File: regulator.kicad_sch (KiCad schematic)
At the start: 20 parts, among them U3 AP62200TWU-7, U4 AP62200TWU-7

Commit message: Ready to restart work!
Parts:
- removed R16: 10k, symbol Device:R
- removed R2: 100k, symbol Device:R
- removed R3: 18k, symbol Device:R
- removed R4: 33k, symbol Device:R
- added R13: 15kΩ, Resistor_SMD:R_0603_1608Metric, symbol !Resistor-0603:15kΩ
- added R2: 20kΩ, Resistor_SMD:R_0603_1608Metric, symbol !Resistor-0603:20kΩ
- added R3: 3.6kΩ, Resistor_SMD:R_0603_1608Metric, symbol !Resistor-0603:3.6kΩ
- added R4: 49.9kΩ, Resistor_SMD:R_0603_1608Metric, symbol !Resistor-0603:49.9kΩ
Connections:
- net +3.3V: now also R4.1
- net +5V: now also R2.1
- net GND: now also R13.2, R3.2
- net at U3.4 (FB): now also R2.2, R3.1
- net at U4.4 (FB): now also R13.1, R4.2

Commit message: Schematic complete (I think)
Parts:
- removed C11, C13, C14, C2, C4, C5: 0.1u, Capacitor_SMD:C_0805_2012Metric, symbol Device:C
- removed C12, C17: 47u, Capacitor_SMD:C_0805_2012Metric, symbol Device:C
- removed C15, C6: 10u, Capacitor_SMD:C_0805_2012Metric, symbol Device:C
- removed C16, C3: 47u, Capacitor_SMD:C_1206_3216Metric, symbol Device:C
- added C10, C6: 10uF, Capacitor_SMD:C_0805_2012Metric, symbol !Capacitor-0805:10uF_X5R_50V
- added C11, C13, C2, C3, C4, C5: 100nF, Capacitor_SMD:C_0603_1608Metric, symbol !Capacitor-0603:100nF_X7R_50V
- added C12, C15, C17, C18: 47uF, Capacitor_SMD:C_0805_2012Metric, symbol !Capacitor-1206:47uF_X5R_10V
- L1, L2: value 6.8uH -> FXL0630-6R8-M; symbol Device:L -> !Inductor-Power:FXL0630-6R8-M; PN FXL0630-6R8-M -> (none)
- U3, U4: symbol motion-sensor-syms:ADP6220x -> !Power Management:AP62200TWU-7
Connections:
- net +3.3V: now also C12.1, C15.1
- net +5V: now also C17.1, C18.1
- net GND: now also C10.2, C11.2, C12.2, C13.2, C15.2, C17.2, C18.2, C2.2, C4.2, C6.2
- net V_{IN}: now also C10.1, C2.1, C4.1, C6.1
- net at L2.1, U4.2 (SW): now also C5.2
- net at U4.6 (BST): now also C5.1
- net at L1.1, U3.2 (SW): now also C3.2
- net at U3.5 (EN): now also C11.1
- net at U3.6 (BST): now also C3.1
- net at U4.5 (EN): now also C13.1

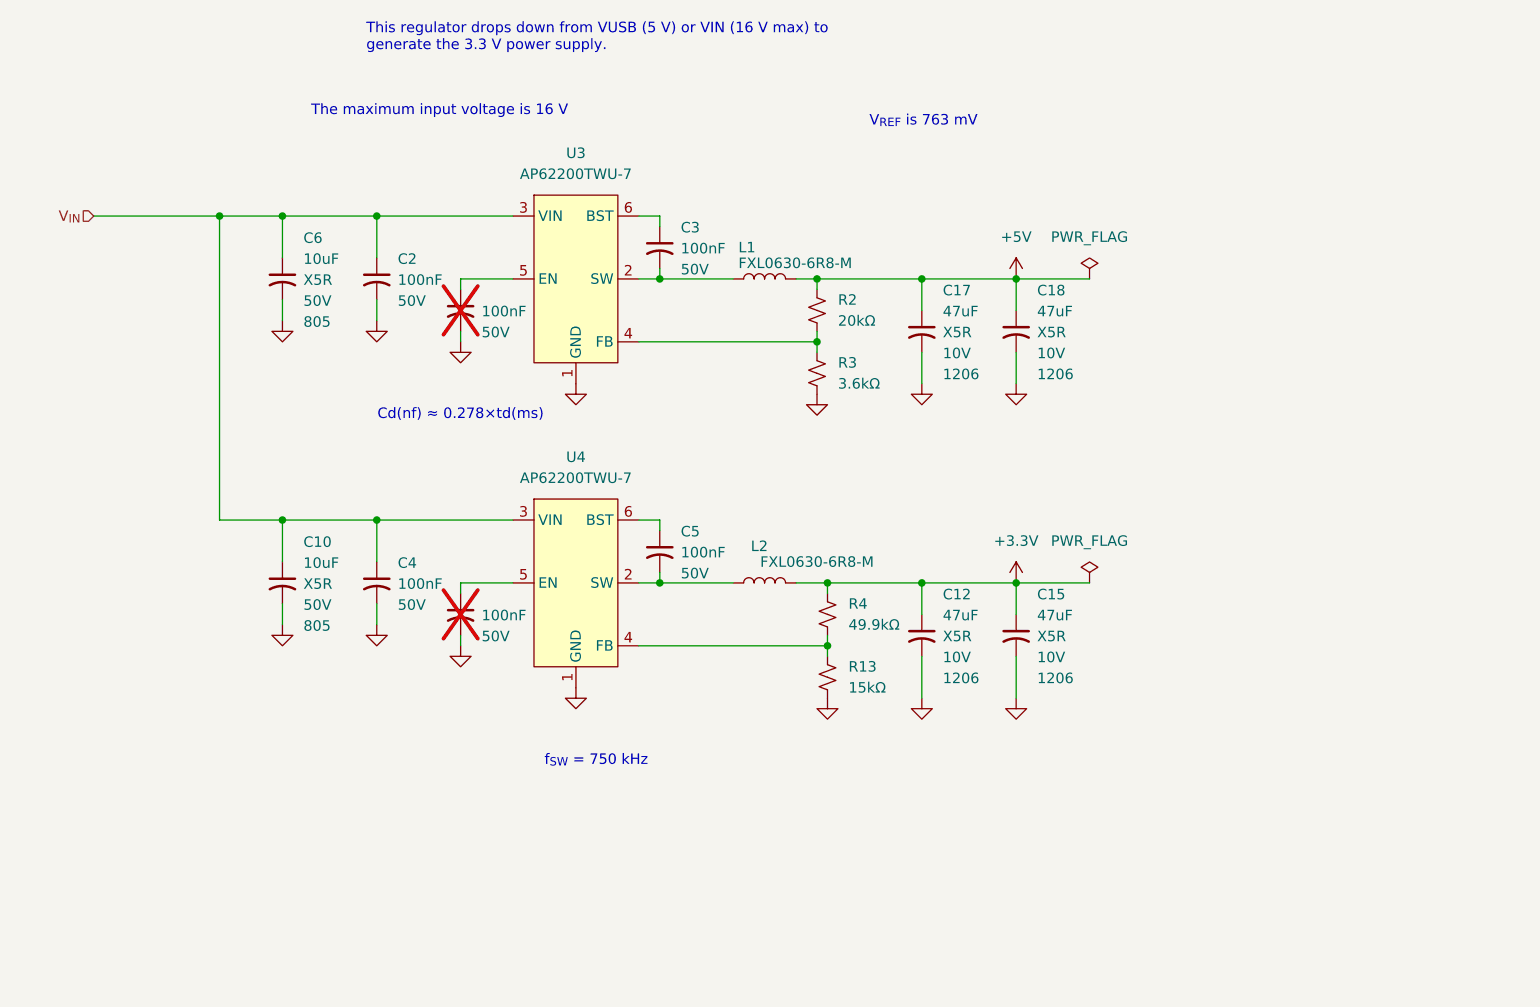
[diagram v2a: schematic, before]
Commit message: Split the two ground planes
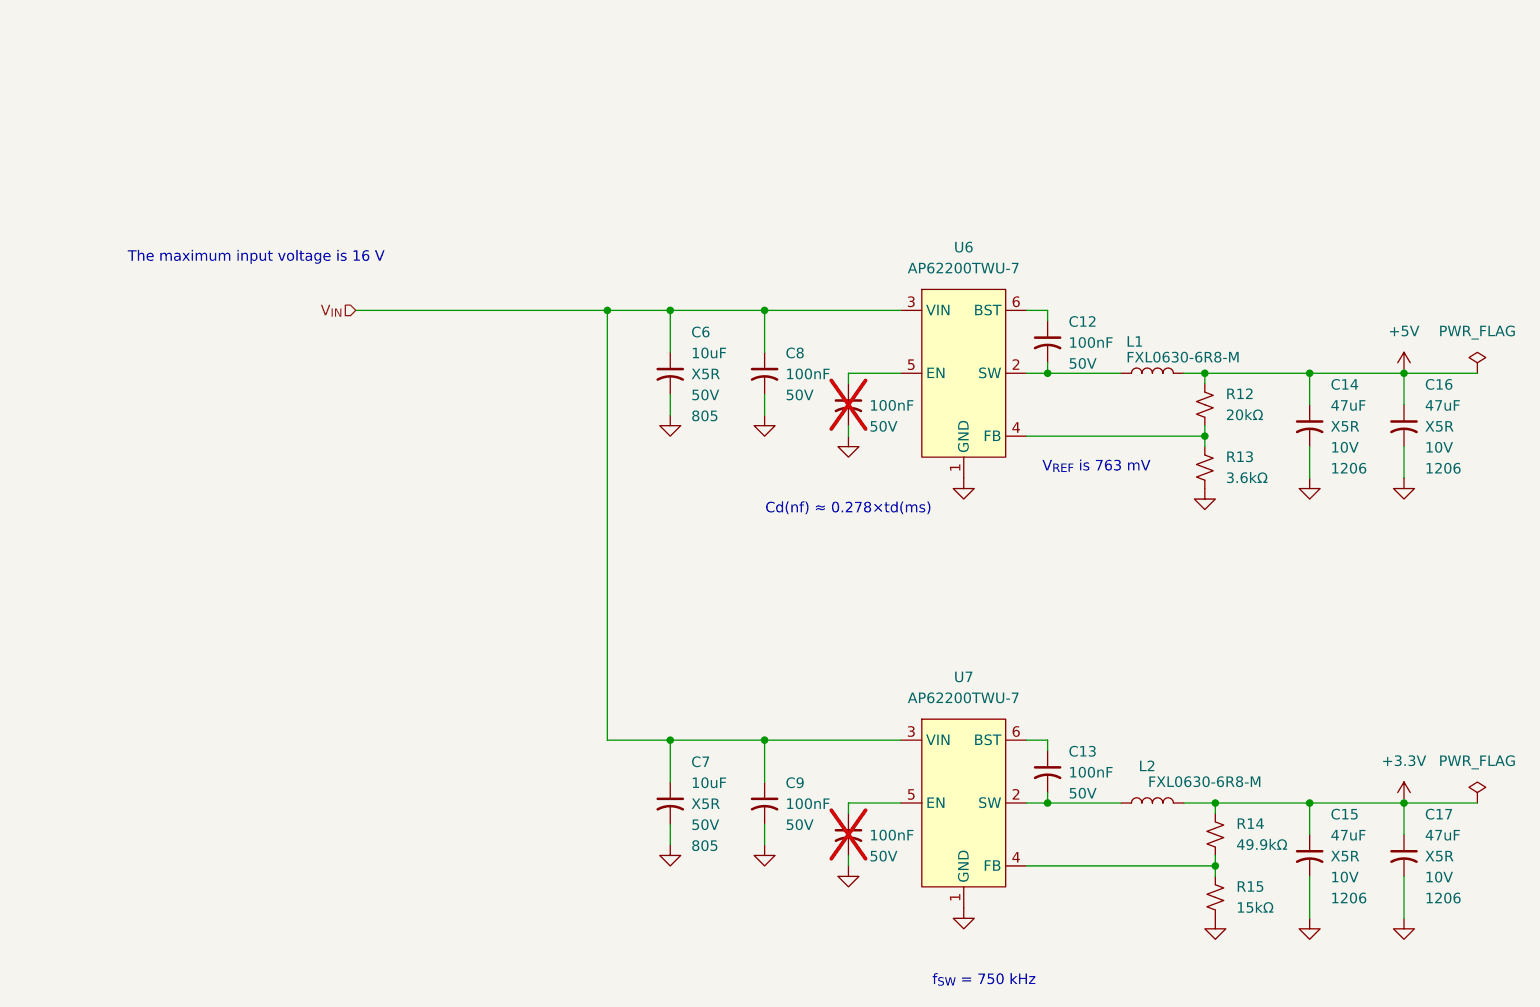
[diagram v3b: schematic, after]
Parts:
- C14: renamed from C17; footprint Capacitor_SMD:C_0805_2012Metric -> Capacitor_SMD:C_1206_3216Metric
- C15: renamed from C12; footprint Capacitor_SMD:C_0805_2012Metric -> Capacitor_SMD:C_1206_3216Metric
- C16: renamed from C18; footprint Capacitor_SMD:C_0805_2012Metric -> Capacitor_SMD:C_1206_3216Metric
- C17: renamed from C15; footprint Capacitor_SMD:C_0805_2012Metric -> Capacitor_SMD:C_1206_3216Metric
- renumbered C11 to C10, C13 to C11, C3 to C12, C5 to C13, C10 to C7, C2 to C8, C4 to C9, R2 to R12, R3 to R13, R4 to R14, R13 to R15, U3 to U6, U4 to U7
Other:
- note removed: "This regulator drops down from VUSB (5 V) or VIN (16 V max) to generate the 3.3 V power supply."
- moved on the sheet: C12, C13, C14, C15, C16, C17, C6, C7, C8, C9, L1, L2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

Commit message: Rev B Submitted
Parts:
- C10, C11, C12, C13, C8, C9: JLCPCB C14663 -> (none); JLCPCB PN (none) -> C14663
- C14, C15, C16, C17: JLCPCB C96123 -> (none); JLCPCB PN (none) -> C96123
- C6, C7: JLCPCB C440198 -> (none); JLCPCB PN (none) -> C440198; Unnamed: 4 (none) -> nan
- L1, L2: JLCPCB C167221 -> (none); JLCPCB PN (none) -> C167221
- R12: JLCPCB C4184 -> (none); JLCPCB PN (none) -> C4184
- R13: JLCPCB C22980 -> (none); JLCPCB PN (none) -> C22980
- R14: JLCPCB C23184 -> (none); JLCPCB PN (none) -> C23184
- R15: JLCPCB C22809 -> (none); JLCPCB PN (none) -> C22809
- U6, U7: FT Rotation Offset (none) -> 90; JLCPCB C2895288 -> (none); JLCPCB PN (none) -> C2895288
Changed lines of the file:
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@@
 	(generator_version "9.0")
 	(paper "A4")
+	(title_block
+		(rev "B")
+	)
 	(text "f_{SW} = 750 kHz"
 		(exclude_from_sim no)
@@
 			)
 		)
-		(property "JLCPCB" "C14663"
+		(property "Tolerance" "±10%"
 			(at 125.73 118.11 0)
 			(effects
@@
 			)
 		)
-		(property "Tolerance" "±10%"
+		(property "JLCPCB PN" "C14663"
 			(at 125.73 118.11 0)
 			(effects
@@
 			)
 		)
-		(property "JLCPCB" "C96123"
+		(property "Tolerance" "±20%"
 			(at 203.2 124.46 0)
 			(effects
@@
 			)
 		)
-		(property "Tolerance" "±20%"
+		(property "JLCPCB PN" "C96123"
 			(at 203.2 124.46 0)
 			(effects
@@
 			)
 		)
-		(property "JLCPCB" "C14663"
+		(property "Tolerance" "±10%"
 			(at 125.73 66.04 0)
 			(effects
@@
 			)
 		)
-		(property "Tolerance" "±10%"
+		(property "JLCPCB PN" "C14663"
 			(at 125.73 66.04 0)
 			(effects
@@
 			)
 		)
-		(property "JLCPCB" "C23184"
+		(property "Power" "100mW"
 			(at 180.34 121.92 0)
 			(effects
@@
 			)
 		)
-		(property "Power" "100mW"
+		(property "Tempco" "±100ppm/℃"
 			(at 180.34 121.92 0)
 			(effects
@@
 			)
 		)
-		(property "Tempco" "±100ppm/℃"
+		(property "JLCPCB PN" "C23184"
 			(at 180.34 121.92 0)
 			(effects
@@
 			)
 		)
-		(property "JLCPCB" "C167221"
+		(property "JLCPCB PN" "C167221"
 			(at 172.72 66.04 0)
 			(effects
@@
 			)
 		)
-		(property "JLCPCB" "C14663"
+		(property "Tolerance" "±10%"
 			(at 135.89 69.85 0)
 			(effects
@@
 			)
 		)
-		(property "Tolerance" "±10%"
+		(property "JLCPCB PN" "C14663"
 			(at 135.89 69.85 0)
 			(effects
@@
 			)
 		)
-		(property "JLCPCB" "C4184"
+		(property "Power" "100mW"
 			(at 179.07 69.85 0)
 			(effects
@@
 			)
 		)
-		(property "Power" "100mW"
+		(property "Tempco" "±100ppm/℃"
 			(at 179.07 69.85 0)
 			(effects
@@
 			)
 		)
-		(property "Tempco" "±100ppm/℃"
+		(property "JLCPCB PN" "C4184"
 			(at 179.07 69.85 0)
 			(effects
@@
 			)
 		)
-		(property "JLCPCB" "C22809"
+		(property "Power" "100mW"
 			(at 180.34 129.54 0)
 			(effects
@@
 			)
 		)
-		(property "Power" "100mW"
+		(property "Tempco" "±100ppm/℃"
 			(at 180.34 129.54 0)
 			(effects
@@
 			)
 		)
-		(property "Tempco" "±100ppm/℃"
+		(property "JLCPCB PN" "C22809"
 			(at 180.34 129.54 0)
 			(effects
@@
 			)
 		)
-		(property "JLCPCB" "C167221"
+		(property "JLCPCB PN" "C167221"
 			(at 172.72 118.11 0)
 			(effects
@@
 			)
 		)
-		(property "JLCPCB" "C14663"
+		(property "Tolerance" "±10%"
 			(at 160.02 114.3 0)
 			(effects
@@
 			)
 		)
-		(property "Tolerance" "±10%"
+		(property "JLCPCB PN" "C14663"
 			(at 160.02 114.3 0)
 			(effects
@@
 			)
 		)
-		(property "JLCPCB" "C96123"
+		(property "Tolerance" "±20%"
 			(at 203.2 72.39 0)
 			(effects
@@
 			)
 		)
-		(property "Tolerance" "±20%"
+		(property "JLCPCB PN" "C96123"
 			(at 203.2 72.39 0)
 			(effects
@@
 			)
 		)
-		(property "JLCPCB" "C96123"
+		(property "Tolerance" "±20%"
 			(at 191.77 72.39 0)
 			(effects
@@
 			)
 		)
-		(property "Tolerance" "±20%"
+		(property "JLCPCB PN" "C96123"
 			(at 191.77 72.39 0)
 			(effects
@@
 			)
 		)
-		(property "JLCPCB" "C96123"
+		(property "Tolerance" "±20%"
 			(at 191.77 124.46 0)
 			(effects
@@
 			)
 		)
-		(property "Tolerance" "±20%"
+		(property "JLCPCB PN" "C96123"
 			(at 191.77 124.46 0)
 			(effects
@@
 			)
 		)
-		(property "JLCPCB" "C2895288"
+		(property "JLCPCB PN" "C2895288"
 			(at 154.94 85.344 0)
 			(effects
@@
 			)
 		)
+		(property "FT Rotation Offset" "90"
+			(at 149.86 66.04 0)
+			(effects
+				(font
+					(size 1.27 1.27)
+				)
+				(hide yes)
+			)
+		)
 		(pin "6"
 		)
@@
 			)
 		)
-		(property "JLCPCB" "C14663"
+		(property "Tolerance" "±10%"
 			(at 135.89 121.92 0)
 			(effects
@@
 			)
 		)
-		(property "Tolerance" "±10%"
+		(property "JLCPCB PN" "C14663"
 			(at 135.89 121.92 0)
 			(effects
@@
 			)
 		)
-		(property "JLCPCB" "C22980"
+		(property "Power" "100mW"
 			(at 179.07 77.47 0)
 			(effects
@@
 			)
 		)
-		(property "Power" "100mW"
+		(property "Tempco" "±100ppm/℃"
 			(at 179.07 77.47 0)
 			(effects
@@
 			)
 		)
-		(property "Tempco" "±100ppm/℃"
+		(property "JLCPCB PN" "C22980"
 			(at 179.07 77.47 0)
 			(effects
@@
 			)
 		)
-		(property "JLCPCB" "C2895288"
+		(property "JLCPCB PN" "C2895288"
 			(at 154.94 137.414 0)
 			(effects
@@
 			)
 		)
+		(property "FT Rotation Offset" "90"
+			(at 149.86 118.11 0)
+			(effects
+				(font
+					(size 1.27 1.27)
+				)
+				(hide yes)
+			)
+		)
 		(pin "6"
 		)
@@
 			)
 		)
-		(property "JLCPCB" "C440198"
+		(property "Tolerance" "±10%"
 			(at 114.3 66.04 0)
 			(effects
@@
 			)
 		)
-		(property "Tolerance" "±10%"
+		(property "JLCPCB PN" "C440198"
+			(at 114.3 66.04 0)
+			(effects
+				(font
+					(size 1.27 1.27)
+				)
+				(hide yes)
+			)
+		)
+		(property "Unnamed: 4" "nan"
 			(at 114.3 66.04 0)
 			(effects
@@
 			)
 		)
-		(property "JLCPCB" "C14663"
+		(property "Tolerance" "±10%"
 			(at 160.02 62.23 0)
 			(effects
@@
 			)
 		)
-		(property "Tolerance" "±10%"
+		(property "JLCPCB PN" "C14663"
 			(at 160.02 62.23 0)
 			(effects
@@
 			)
 		)
-		(property "JLCPCB" "C440198"
+		(property "Tolerance" "±10%"
 			(at 114.3 118.11 0)
 			(effects
@@
 			)
 		)
-		(property "Tolerance" "±10%"
+		(property "JLCPCB PN" "C440198"
+			(at 114.3 118.11 0)
+			(effects
+				(font
+					(size 1.27 1.27)
+				)
+				(hide yes)
+			)
+		)
+		(property "Unnamed: 4" "nan"
 			(at 114.3 118.11 0)
 			(effects

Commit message: Got 3D export working
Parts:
- L1, L2: footprint Inductor_SMD:L_Changjiang_FXL0630 -> !Inductors:L_Changjiang_FXL0630
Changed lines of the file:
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@@
 			)
 		)
-		(property "Footprint" "Inductor_SMD:L_Changjiang_FXL0630"
+		(property "Footprint" "!Inductors:L_Changjiang_FXL0630"
 			(at 172.72 66.04 0)
 			(effects
@@
 			)
 		)
-		(property "Footprint" "Inductor_SMD:L_Changjiang_FXL0630"
+		(property "Footprint" "!Inductors:L_Changjiang_FXL0630"
 			(at 172.72 118.11 0)
 			(effects
